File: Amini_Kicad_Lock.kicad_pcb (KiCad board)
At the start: 2 copper layers, 36 parts, among them U1 nRF5340-QKxx, X1 32MHz, X2 32.768kHz

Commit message: 2. commit
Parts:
- removed C2, C3: 1.0µF, Nordic_Semiconductor:CAPC1005X04L
- removed C20: 0.5pF, Nordic_Semiconductor:CAPC0603X03L_C
- removed L1: 2.2nH, Nordic_Semiconductor:INDC0603X03L_C
- added J1: Conn_01x02, Connector_JST:JST_SH_BM02B-SRSS-TB_1x02-1MP_P1.00mm_Vertical, F.Cu at (110.8, 74.4)
- added J2: Conn_01x04, Connector_JST:JST_SH_SM04B-SRSS-TB_1x04-1MP_P1.00mm_Horizontal, F.Cu at (131.5, 62.0)
- added J3: MM8130-2600RA2, MM8130-2600RA2 antenna:MURATA_MM8130-2600RA2, F.Cu at (121.9, 75.4)
- added TP1: TestPoint, TestPoint:TestPoint_Pad_D1.0mm, F.Cu at (123.0, 71.7)
- added TP11: TestPoint, TestPoint:TestPoint_Pad_D1.0mm, F.Cu at (125.7, 69.5)
- added TP14: TestPoint, TestPoint:TestPoint_Pad_D1.0mm, F.Cu at (125.7, 71.6)
- C1: value 0.7pF -> 1.0µF; footprint Nordic_Semiconductor:CAPC0603X03L_C -> Nordic_Semiconductor:CAPC1005X04L
- C10: value 100nF -> 0.7pF; footprint Nordic_Semiconductor:CAPC0603X03L_C -> Inductor_SMD:L_0603_1608Metric
- C16: value 1.0µF -> 100nF; footprint Nordic_Semiconductor:CAPC1005X04L -> Nordic_Semiconductor:CAPC0603X03L_C
- C18: value N.C. -> 100nF; footprint Nordic_Semiconductor:CAPC0603X03L_C_NC -> Nordic_Semiconductor:CAPC0603X03L_C
- C19: value N.C. -> 1.0µF; footprint Capacitor_SMD:C_0201_0603Metric_Pad0.64x0.40mm_HandSolder -> Nordic_Semiconductor:CAPC1005X04L
- C4: value 2.2nF -> N.C.; footprint Nordic_Semiconductor:CAPC0603X03L_C -> Inductor_SMD:L_0603_1608Metric
- C7: value 1.0µF -> 2.2nF; footprint Nordic_Semiconductor:CAPC1005X04L -> Nordic_Semiconductor:CAPC0603X03L_C
- C8, C9: value 100nF -> 1.0µF; footprint Nordic_Semiconductor:CAPC0603X03L_C -> Nordic_Semiconductor:CAPC1005X04L
- L3: value 10µH -> 2.2nH; footprint Nordic_Semiconductor:INDC1608X06L -> Inductor_SMD:L_0603_1608Metric
- L4: value 3.3nH -> 10µH; footprint Nordic_Semiconductor:INDC0603X03L_C -> Nordic_Semiconductor:INDC1608X06L
- TP12: footprint TestPoint:TestPoint_Pad_1.0x1.0mm -> TestPoint:TestPoint_Pad_D1.0mm
- moved L4 15.6 mm to (135.6, 74.9)
- moved L3 14.9 mm to (118.6, 75.3), turned to 90 degrees
- moved C19 14.9 mm to (133.1, 72.1)
- moved C4 11.8 mm to (115.5, 74.2), turned to 180 degrees
- moved C10 8.29 mm to (115.5, 76.7), turned to 0 degrees
- moved A1 6.24 mm to (124.6, 78.5), turned to 0 degrees
- moved TP12 3.47 mm to (123.0, 69.4)
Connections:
- C1 pad 1: GND -> VDD_nRF
- C1 pad 2: Net-(U1-ANT) -> GND
- C10 pad 1: VDD_nRF -> GND
- C10 pad 2: GND -> Net-(U1-ANT)
- C16 pad 1: GND -> VDD_nRF
- C16 pad 2: VDD_nRF -> GND
- C18 pad 1: GND -> VDD_nRF
- C18 pad 2: (no net) -> GND
- C19 pad 2: (no net) -> VDD_nRF
- C4 pad 1: Net-(U1-DECR) -> GND
- C4 pad 2: GND -> Net-(C4-Pad2)
- C5 pad 2: Net-(U1-DECD) -> Net-(U1-DECR)
- C7 pad 1: GND -> Net-(U1-DECR)
- C7 pad 2: Net-(U1-DECA) -> GND
- C8 pad 1: VDD_nRF -> GND
- C8 pad 2: GND -> Net-(U1-DECD)
- C9 pad 1: VDD_nRF -> GND
- C9 pad 2: GND -> Net-(U1-DECA)
- L3 pad 1: Net-(U1-DECD) -> Net-(U1-ANT)
- L3 pad 2: Net-(U1-DCCD) -> Net-(C4-Pad2)
- L4 pad 1: Net-(A1-Pad1) -> Net-(U1-DECD)
- L4 pad 2: (no net) -> Net-(U1-DCCD)
- TP12 pad 1: (no net) -> /SWDIO
- U1 pad AK10: (no net) -> unconnected-(U1-IO2/P0.15-PadAK10)
- U1 pad AK12: (no net) -> unconnected-(U1-SCK/P0.17-PadAK12)
- U1 pad AK14: (no net) -> unconnected-(U1-CSN/P0.18-PadAK14)
- U1 pad AK30: (no net) -> unconnected-(U1-AIN6/P0.27-PadAK30)
- U1 pad AK8: (no net) -> unconnected-(U1-IO1/P0.14-PadAK8)
- U1 pad AL27: (no net) -> unconnected-(U1-P0.24-PadAL27)
- U1 pad AL29: (no net) -> unconnected-(U1-AIN5/P0.26-PadAL29)
- U1 pad AL5: (no net) -> unconnected-(U1-IO0/P0.13-PadAL5)
- U1 pad AL9: (no net) -> unconnected-(U1-IO3/P0.16-PadAL9)
- U1 pad B22: (no net) -> unconnected-(U1-P0.31-PadB22)
- U1 pad G1: GND -> unconnected-(U1-NC-PadG1)
- U1 pad H2: GND -> unconnected-(U1-NC-PadH2)
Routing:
- net VDD_nRF: track 0.00 -> 45.9 mm
- net GND: track 0.00 -> 24.6 mm
- net Net-(JP1-A): track 0.00 -> 7.26 mm
- net Net-(U1-DECR): track 0.00 -> 7.00 mm
- net Net-(U1-DECD): track 0.00 -> 5.65 mm
- net Net-(U1-XL2/P0.01): track 0.00 -> 5.35 mm
- net /XC1: track 0.00 -> 5.35 mm
- net /XC2: track 0.00 -> 4.81 mm
- net Net-(U1-DCCD): track 0.00 -> 4.80 mm
- net Net-(U1-XL1/P0.00): track 0.00 -> 3.79 mm
- net Net-(U1-DCC): track 0.00 -> 3.41 mm
- net Net-(U1-ANT): track 0.00 -> 3.21 mm
- net Net-(U1-DECA): track 0.00 -> 2.88 mm
- net /P0.30: track 0.00 -> 1.55 mm
- net Net-(A1-Pad1): track 0.00 -> 1.46 mm
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
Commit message: 3. commit
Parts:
- moved J2 7.08 mm to (138.3, 60.0)
- moved JP1 1.61 mm to (126.3, 59.4)
- moved LED1 1.61 mm to (127.5, 62.9)
- moved LED2 1.61 mm to (126.6, 65.5)
- moved LED3 1.61 mm to (126.7, 67.4)
- moved R1 1.61 mm to (126.9, 61.1)
- moved R2 1.61 mm to (126.9, 64.7)
- moved R3 1.61 mm to (126.9, 66.7)
- moved C18 0.80 mm to (123.0, 67.2)
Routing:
- net VDD_nRF: track 45.9 -> 0.00 mm
- net GND: track 24.6 -> 0.00 mm
- net Net-(JP1-A): track 7.26 -> 0.00 mm
- net Net-(U1-DECR): track 7.00 -> 0.00 mm
- net Net-(U1-DECD): track 5.65 -> 0.00 mm
- net Net-(U1-XL2/P0.01): track 5.35 -> 0.00 mm
- net /XC1: track 5.35 -> 0.00 mm
- net /XC2: track 4.81 -> 0.00 mm
- net Net-(U1-DCCD): track 4.80 -> 0.00 mm
- net Net-(U1-XL1/P0.00): track 3.79 -> 0.00 mm
- net Net-(U1-DCC): track 3.41 -> 0.00 mm
- net Net-(U1-ANT): track 3.21 -> 0.00 mm
- net Net-(U1-DECA): track 2.88 -> 0.00 mm
- net /P0.30: track 1.55 -> 0.00 mm
- net Net-(A1-Pad1): track 1.46 -> 0.00 mm
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
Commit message: clear, every component on place, wrong with shematic
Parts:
- removed C19: 1.0µF, Nordic_Semiconductor:CAPC1005X04L
- removed L4: 10µH, Nordic_Semiconductor:INDC1608X06L
- added C10: 100nF, Nordic_Semiconductor:CAPC0603X03L_C, F.Cu at (172.6, 64.4)
- added C2: 1.0µF, Nordic_Semiconductor:CAPC1005X04L, F.Cu at (178.3, 58.0)
- added C3: 1.0µF, Nordic_Semiconductor:CAPC1005X04L, F.Cu at (178.7, 56.5)
- added C4: 2.2nF, Nordic_Semiconductor:CAPC0603X03L_C, F.Cu at (182.4, 59.4)
- added L1: 2.2nH, Nordic_Semiconductor:INDC0603X03L_C, F.Cu at (184.5, 61.6)
- added L3: 10µH, Nordic_Semiconductor:INDC1608X06L, F.Cu at (176.3, 56.0)
- added TP3: TestPoint, TestPoint:TestPoint_Pad_D1.0mm, F.Cu at (190.2, 65.2)
- added TP4: TestPoint, TestPoint:TestPoint_Pad_D1.0mm, F.Cu at (190.2, 68.2)
- added TP5: TestPoint, TestPoint:TestPoint_Pad_D1.0mm, F.Cu at (190.2, 71.3)
- C1: value 1.0µF -> 0.7pF; footprint Nordic_Semiconductor:CAPC1005X04L -> Nordic_Semiconductor:CAPC0603X03L_C
- C10: value 0.7pF -> 100nF
- C16: value 100nF -> 1.0µF; footprint Nordic_Semiconductor:CAPC0603X03L_C -> Nordic_Semiconductor:CAPC1005X04L
- C18: value 100nF -> N.C.; footprint Nordic_Semiconductor:CAPC0603X03L_C -> Nordic_Semiconductor:CAPC0603X03L_C_NC
- C4: value N.C. -> 2.2nF
- C7: value 2.2nF -> 1.0µF; footprint Nordic_Semiconductor:CAPC0603X03L_C -> Nordic_Semiconductor:CAPC1005X04L
- C8, C9: value 1.0µF -> 100nF; footprint Nordic_Semiconductor:CAPC1005X04L -> Nordic_Semiconductor:CAPC0603X03L_C
- L3: value 2.2nH -> 10µH
- moved C18 61.6 mm to (184.4, 62.5)
- moved C12 60.8 mm to (179.3, 66.5)
- moved C8 60.8 mm to (172.6, 59.5)
- moved C11 60.8 mm to (176.3, 66.5)
- moved C14 60.8 mm to (181.8, 58.9)
- moved C15 60.8 mm to (181.8, 57.4)
- moved C5 60.8 mm to (174.8, 55.6)
- moved C6 60.8 mm to (179.0, 57.6)
- moved C7 60.8 mm to (174.3, 56.5)
- moved C9 60.8 mm to (172.5, 61.9)
- moved U1 60.8 mm to (177.2, 61.8)
- moved X1 60.8 mm to (184.3, 60.3)
- moved C1 60.8 mm to (181.9, 60.4)
- moved C16 60.8 mm to (174.6, 53.9)
- moved C17 60.8 mm to (171.9, 58.7)
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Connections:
- C1 pad 1: VDD_nRF -> GND
- C1 pad 2: GND -> Net-(U1-ANT)
- C10 pad 1: GND -> VDD_nRF
- C10 pad 2: Net-(U1-ANT) -> GND
- C16 pad 1: VDD_nRF -> GND
- C16 pad 2: GND -> VDD_nRF
- C18 pad 1: VDD_nRF -> GND
- C18 pad 2: GND -> Net-(C18-Pad2)
- C4 pad 1: GND -> Net-(U1-DECR)
- C4 pad 2: Net-(C4-Pad2) -> GND
- C5 pad 2: Net-(U1-DECR) -> Net-(U1-DECD)
- C7 pad 1: Net-(U1-DECR) -> GND
- C7 pad 2: GND -> Net-(U1-DECA)
- C8 pad 1: GND -> VDD_nRF
- C8 pad 2: Net-(U1-DECD) -> GND
- C9 pad 1: GND -> VDD_nRF
- C9 pad 2: Net-(U1-DECA) -> GND
- J3 pad IN: Net-(C4-Pad2) -> Net-(C18-Pad2)
- L3 pad 1: Net-(U1-ANT) -> Net-(U1-DECD)
- L3 pad 2: Net-(C4-Pad2) -> Net-(U1-DCCD)
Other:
- board outline added: 29 x 20.1 mm

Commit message: clear, every component on place, component match kicad
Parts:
- removed the C1 at (181.9, 60.4)
- removed C17: 100nF, Nordic_Semiconductor:CAPC0603X03L_C
- removed the C18 at (184.4, 62.5)
- removed the L1 at (184.5, 61.6)
- removed TP11, TP12, TP14: TestPoint, TestPoint:TestPoint_Pad_D1.0mm
- C1: renamed from C4; value 2.2nF -> 0.7pF
- C18: renamed from C10; value 100nF -> N.C.
- L1: renamed from L3; value 10µH -> 2.2nH
- moved TP3 7.14 mm to (183.0, 65.0)
- moved TP5 6.13 mm to (185.6, 67.2)
- moved TP4 5.48 mm to (185.7, 65.0)
- moved C1 0.92 mm to (175.5, 68.3)
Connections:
- C1 pad 1: Net-(U1-DECR) -> GND
- C1 pad 2: GND -> Net-(U1-ANT)
- C18 pad 1: VDD_nRF -> GND
- C18 pad 2: GND -> Net-(C18-Pad2)
- L1 pad 1: Net-(U1-DECD) -> Net-(U1-ANT)
- L1 pad 2: Net-(U1-DCCD) -> Net-(C18-Pad2)

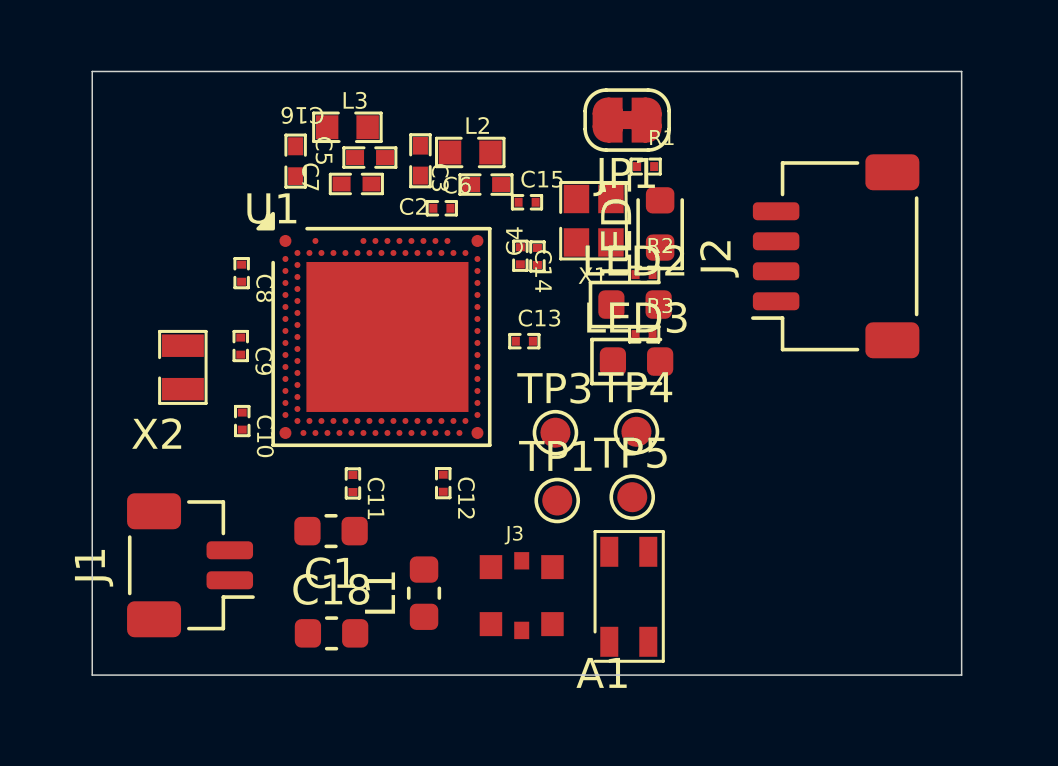
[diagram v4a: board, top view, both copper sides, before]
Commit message: mousebites added
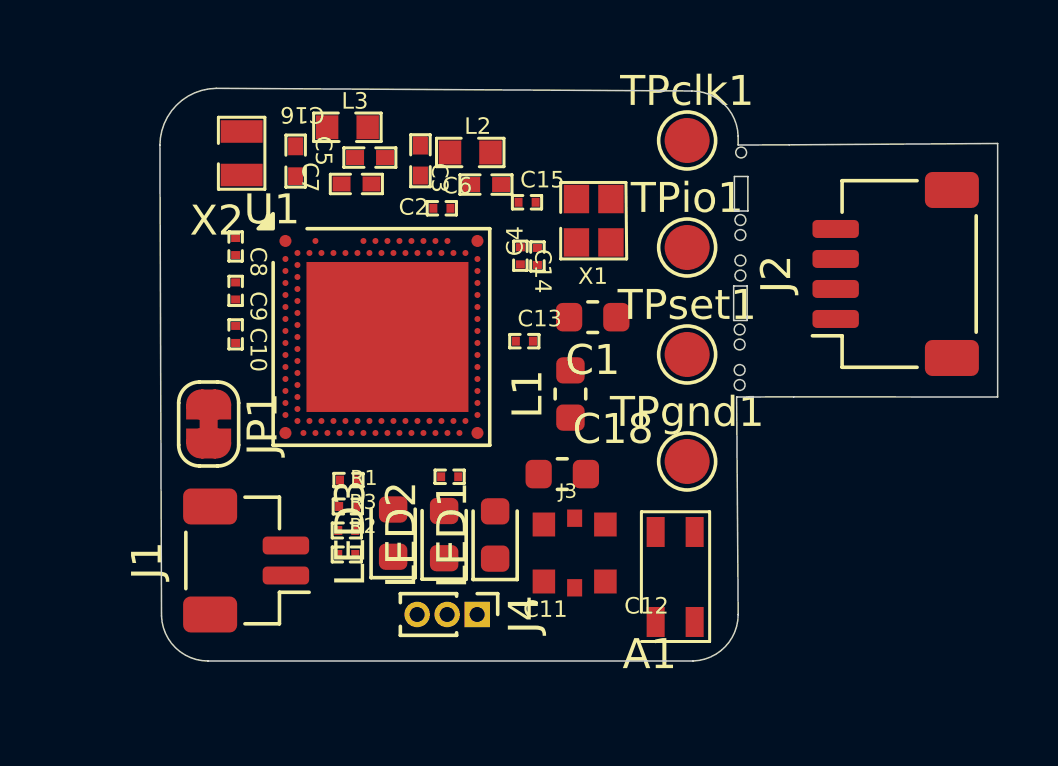
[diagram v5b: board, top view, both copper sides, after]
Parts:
- removed TP1, TP3, TP4, TP5: TestPoint, TestPoint:TestPoint_Pad_D1.0mm
- added J4: Conn_01x03_Pin, Connector_PinHeader_1.00mm:PinHeader_1x03_P1.00mm_Vertical, F.Cu at (180.4, 71.1)
- added TPclk1: TestPoint, TestPoint:TestPoint_Pad_D1.5mm, F.Cu at (187.4, 55.3)
- added TPgnd1: TestPoint, TestPoint:TestPoint_Pad_D1.5mm, F.Cu at (187.4, 66.0)
- added TPio1: TestPoint, TestPoint:TestPoint_Pad_D1.5mm, F.Cu at (187.4, 58.9)
- added TPset1: TestPoint, TestPoint:TestPoint_Pad_D1.5mm, F.Cu at (187.4, 62.4)
- moved JP1 17.2 mm to (171.4, 64.8), turned to -90 degrees
- moved R1 15.1 mm to (176.0, 67.7)
- moved R2 13.6 mm to (176.0, 69.2)
- moved R3 11.9 mm to (176.0, 68.5)
- moved LED1 11.7 mm to (181.0, 68.5)
- moved C1 11.3 mm to (184.3, 61.2)
- moved LED2 9.96 mm to (179.3, 68.4), turned to 90 degrees
- moved LED3 9.93 mm to (177.6, 68.4), turned to 90 degrees
- moved C18 9.35 mm to (183.2, 66.4)
- moved L1 8.24 mm to (183.5, 63.8)
- moved X2 7.40 mm to (171.7, 58.5)
- moved C10 2.90 mm to (172.3, 61.5)
- moved J3 2.27 mm to (183.7, 69.0)
- moved J2 2.07 mm to (194.3, 59.8)
- moved J1 1.88 mm to (172.7, 69.3)
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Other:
- board size 29 x 20.1 mm -> 27.9 x 19.1 mm

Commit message: backup before rework stackable boards
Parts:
- turned JP1 to 90 degrees
- turned L1 to -90 degrees
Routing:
- net (no net): track 0.00 -> 38.1 mm

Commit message: backup mid routing
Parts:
- added D1: D, Diode_SMD:D_0402_1005Metric_Pad0.77x0.64mm_HandSolder, F.Cu at (179.8, 54.4)
- C7: footprint Nordic_Semiconductor:CAPC1005X04L -> Capacitor_SMD:C_0402_1005Metric
- J1: value Conn_01x02 -> Conn_01x02_Pin; footprint Connector_JST:JST_SH_BM02B-SRSS-TB_1x02-1MP_P1.00mm_Vertical -> Connector_PinHeader_2.00mm:PinHeader_1x02_P2.00mm_Vertical
- J4: footprint Connector_PinHeader_1.00mm:PinHeader_1x03_P1.00mm_Vertical -> Connector_PinHeader_2.00mm:PinHeader_1x03_P2.00mm_Vertical
- moved J1 18.3 mm to (184.6, 55.3), turned to -90 degrees
- moved JP1 3.80 mm to (173.2, 68.1)
- moved LED1 3.56 mm to (180.1, 71.9), turned to 0 degrees
- moved C2 3.54 mm to (176.2, 55.1), turned to -90 degrees
- moved C4 3.33 mm to (185.7, 60.0), turned to 180 degrees
- moved J4 3.30 mm to (177.1, 71.2)
- moved C3 3.20 mm to (180.9, 54.2), turned to 180 degrees
- moved C10 3.15 mm to (172.2, 64.7)
- moved X1 2.91 mm to (182.1, 58.3), turned to -90 degrees
- moved C9 2.22 mm to (172.3, 62.3), turned to 90 degrees
- moved C7 2.12 mm to (176.4, 56.7), turned to 0 degrees
- moved LED2 2.11 mm to (180.1, 70.4), turned to 0 degrees
- moved C6 1.87 mm to (179.8, 55.9), turned to 90 degrees
- moved R2 1.83 mm to (175.8, 67.4), turned to 180 degrees
- moved L2 1.71 mm to (179.1, 57.9)
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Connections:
- J1 pad 2: VDD_nRF -> Net-(D1-A)
- U1 pad A25: unconnected-(U1-NC-PadA25) -> GND
- U1 pad B26: unconnected-(U1-NC-PadB26) -> GND
- U1 pad F2: unconnected-(U1-NC-PadF2) -> GND
- U1 pad G1: unconnected-(U1-NC-PadG1) -> GND
- U1 pad H2: unconnected-(U1-NC-PadH2) -> GND
- U1 pad J1: unconnected-(U1-DCCH-PadJ1) -> GND
- X1 pad 4: unconnected-(X1-GND-Pad4) -> GND
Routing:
- net VDD_nRF: track 0.00 -> 71.6 mm, vias 0 -> 10
- net GND: track 0.00 -> 45.2 mm, vias 0 -> 37
- net (no net): track 38.1 -> 0.00 mm
- net /SWDCLK: track 0.00 -> 18.3 mm, vias 0 -> 2
- net /SWDIO: track 0.00 -> 14.5 mm, vias 0 -> 2
- net /~{RESET}: track 0.00 -> 13.4 mm
- net Net-(U1-XL1/P0.00): track 0.00 -> 8.59 mm, vias 0 -> 2
- net /XC2: track 0.00 -> 8.22 mm
- net Net-(U1-XL2/P0.01): track 0.00 -> 6.96 mm, vias 0 -> 2
- net Net-(U1-DECR): track 0.00 -> 6.70 mm, vias 0 -> 2
- net Net-(U1-DCCD): track 0.00 -> 4.82 mm
- net Net-(U1-DECD): track 0.00 -> 4.68 mm
- net /XC1: track 0.00 -> 3.87 mm
- net Net-(U1-DECN): track 0.00 -> 3.52 mm
- net Net-(U1-DECA): track 0.00 -> 2.10 mm
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- added copper zone on B.Cu, net GND
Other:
- board size 27.9 x 19.1 mm -> 25.7 x 19.1 mm

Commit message: backup almoast done routing - new space reorientation led
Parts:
- moved LED2 4.08 mm to (176.4, 68.5), turned to 90 degrees
- moved LED1 4.01 mm to (177.9, 68.5), turned to 90 degrees
- moved A1 3.89 mm to (182.9, 70.1), turned to -90 degrees
- moved C11 3.54 mm to (179.0, 66.8), turned to -90 degrees
- moved R1 3.41 mm to (178.0, 66.5)
- moved LED3 2.73 mm to (174.9, 68.5)
- moved J3 2.06 mm to (182.1, 70.3), turned to 90 degrees
- moved R3 1.95 mm to (175.1, 66.5)
- moved C12 1.28 mm to (180.4, 66.8), turned to 180 degrees
- moved R2 1.12 mm to (176.5, 66.5)
- moved TPgnd1 0.75 mm to (187.4, 64.6)
- moved C18 0.73 mm to (182.8, 67.0), turned to 90 degrees
- moved TPset1 0.50 mm to (187.4, 61.5)
- moved J4 0.36 mm to (177.0, 71.6)
- moved JP1 0.34 mm to (172.9, 68.2)
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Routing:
- net /P0.29: track 0.00 -> 8.50 mm
- net Net-(JP1-A): track 0.00 -> 7.24 mm
- net /P0.28/AIN7: track 0.00 -> 7.01 mm
- net VDD_nRF: track 71.6 -> 77.3 mm, vias 10 -> 11
- net Net-(C18-Pad2): track 0.00 -> 3.27 mm
- net /P0.30: track 0.00 -> 3.07 mm
- net Net-(A1-Pad1): track 0.00 -> 1.26 mm
- net Net-(LED3-A): track 0.00 -> 1.21 mm
- net Net-(LED2-A): track 0.00 -> 1.17 mm
- net Net-(LED1-A): track 0.00 -> 1.17 mm
- net GND: track 45.2 -> 44.4 mm
- net (no net): vias 0 -> 2
